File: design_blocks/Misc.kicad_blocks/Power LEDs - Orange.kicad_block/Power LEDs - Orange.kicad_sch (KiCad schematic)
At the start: 6 parts

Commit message: Fixed footprint on LED block; added Roxy 6.5
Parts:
- JP4: footprint (none) -> CRGM Connector:SolderJumper-2_P1.3mm_Bridged_RoundedPad1.0x1.5mm
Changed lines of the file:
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@@
 			)
 		)
-		(property "Footprint" ""
+		(property "Footprint" "CRGM Connector:SolderJumper-2_P1.3mm_Bridged_RoundedPad1.0x1.5mm"
 			(at 161.29 46.99 0)
 			(effects

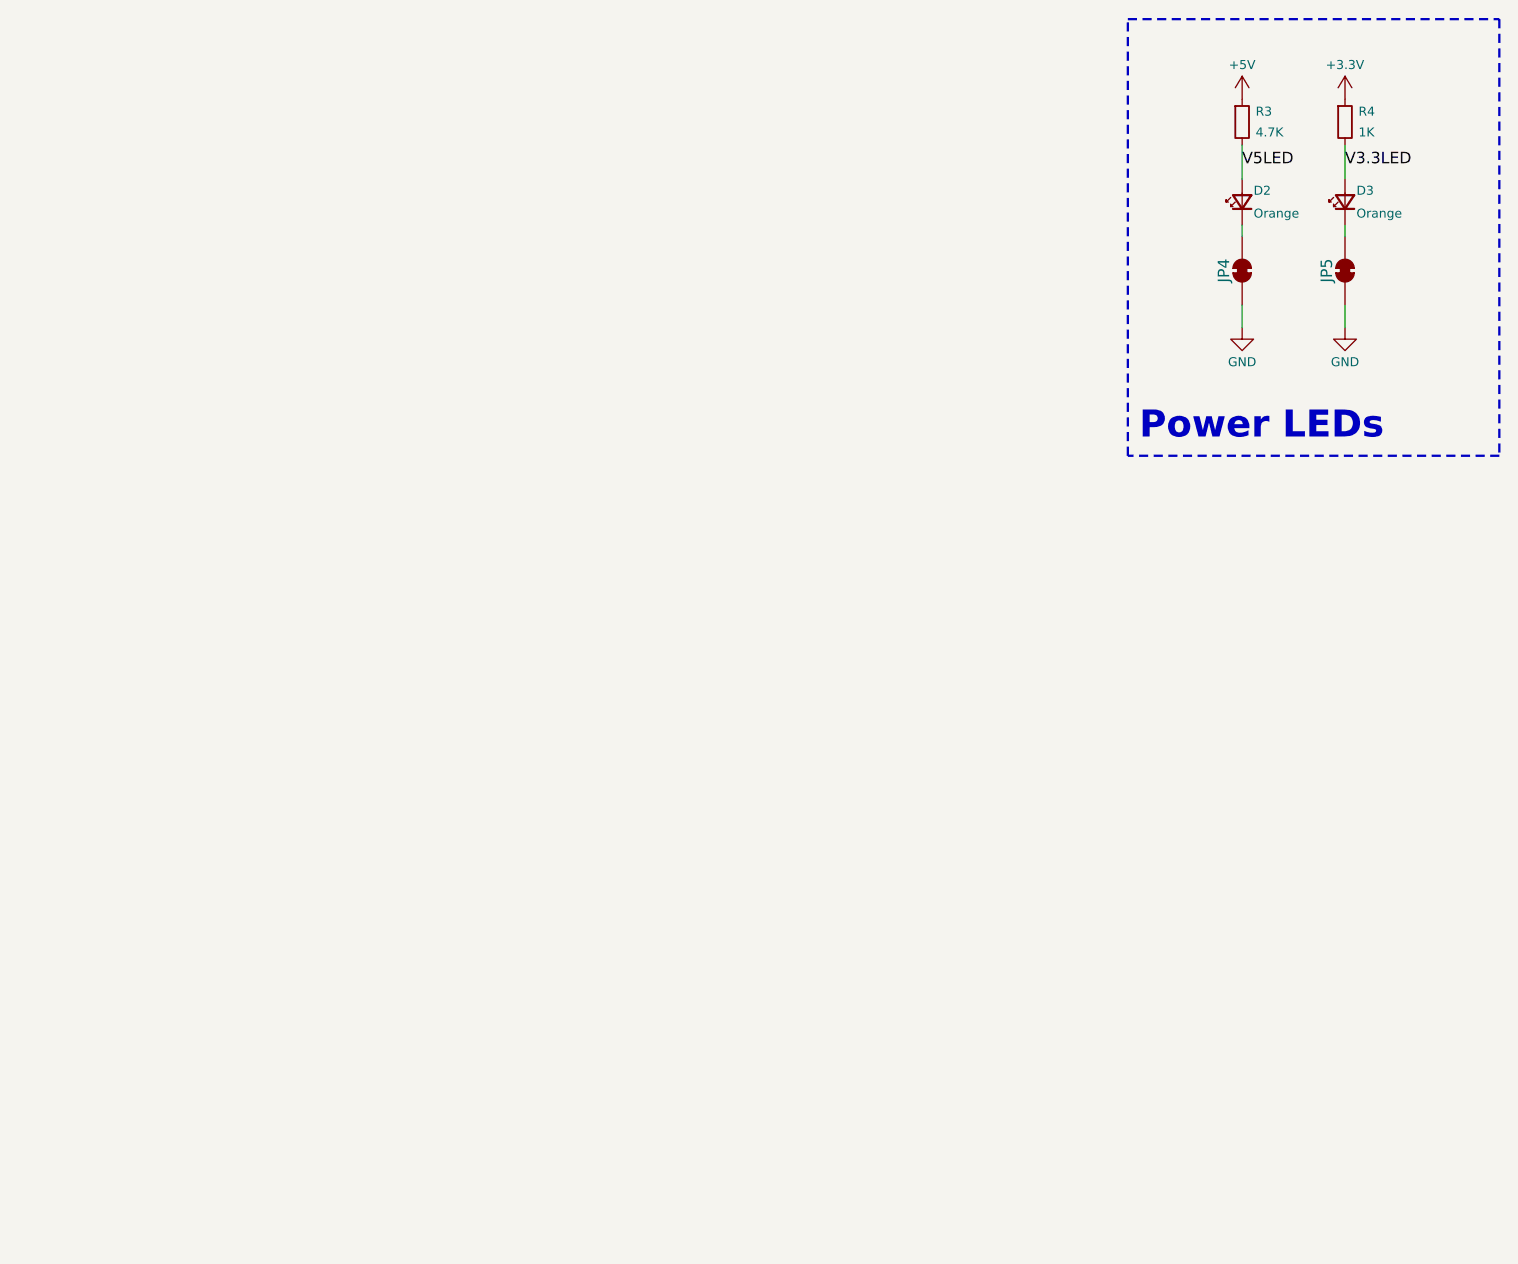
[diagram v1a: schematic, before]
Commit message: Updated blocks
Added current sensor
Updated LEDs
Updated QWICC
Changed MCU
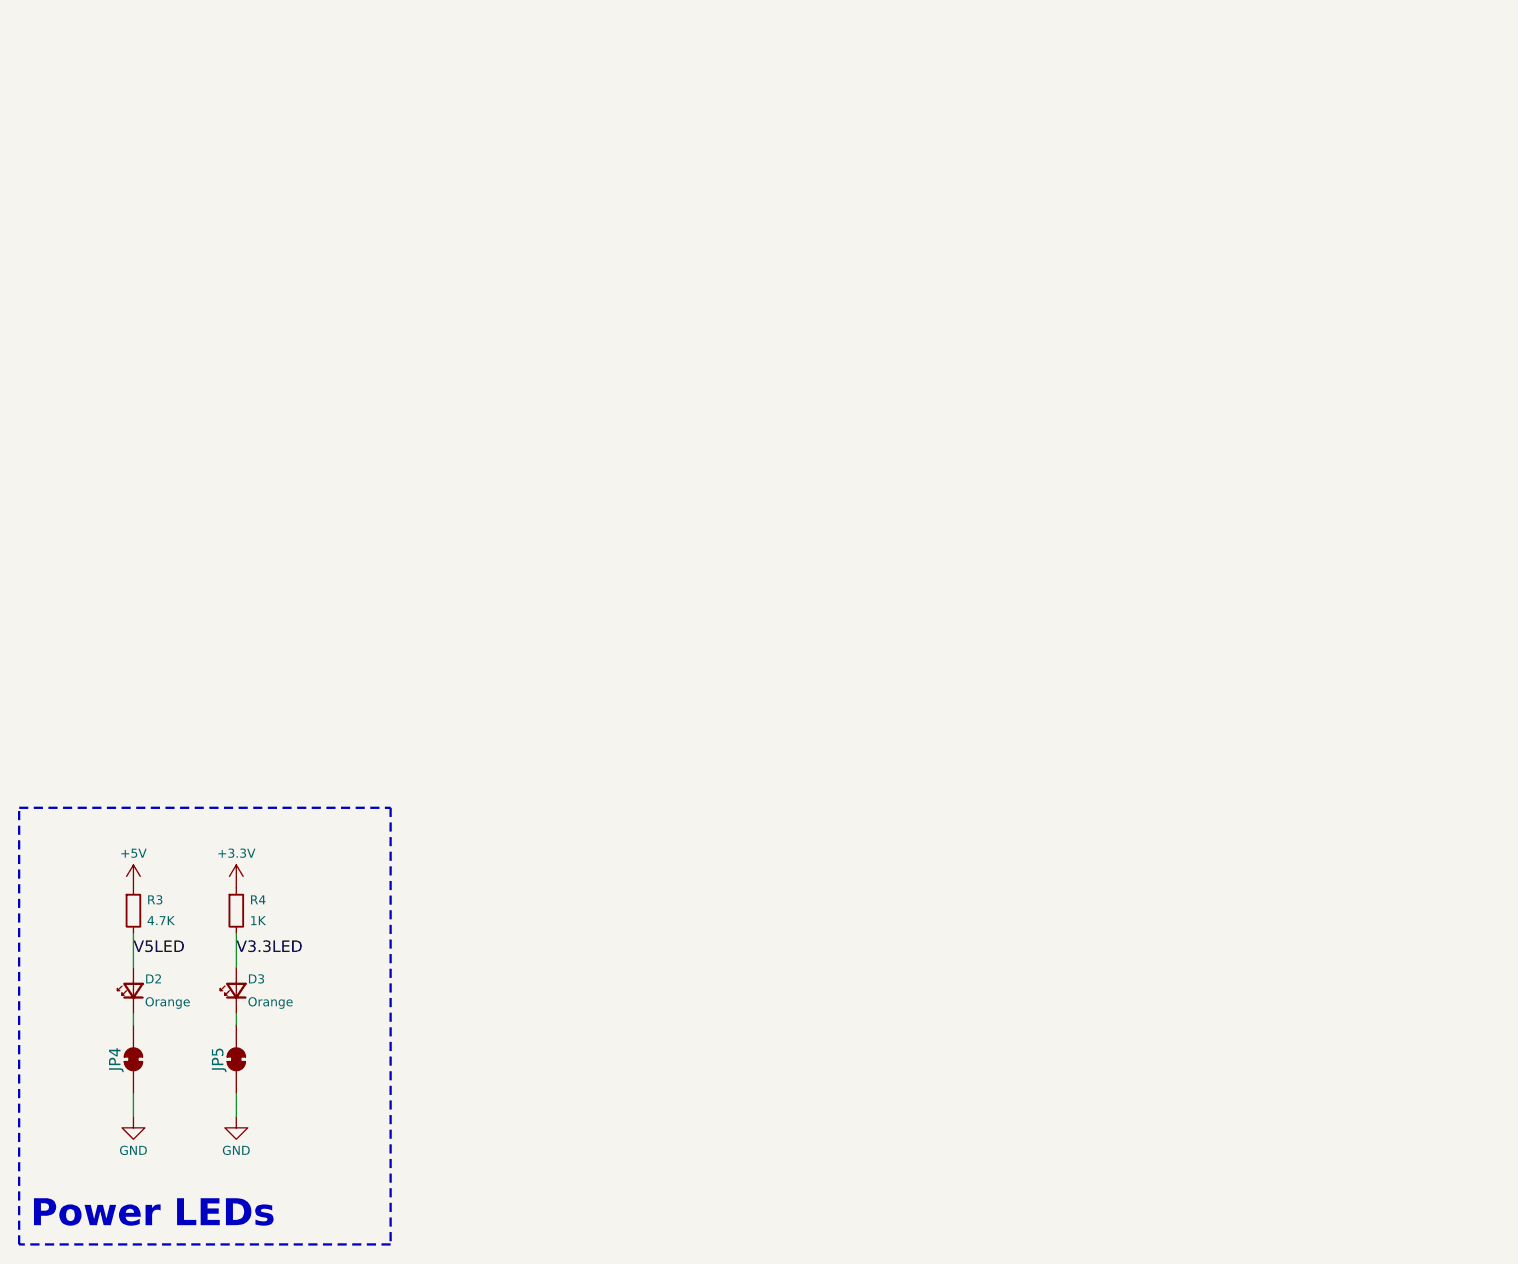
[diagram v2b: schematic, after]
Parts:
- D2, D3: footprint LED_SMD:LED_0603_1608Metric -> CRGM Passive:LED_0603_1608Metric
- R3, R4: footprint Resistor_SMD:R_0603_1608Metric -> CRGM Passive:R_0603_1608Metric
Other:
- moved on the sheet: D2, D3, JP4, JP5, R3, R4
